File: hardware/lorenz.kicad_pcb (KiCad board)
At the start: 2 copper layers, 100 x 100 mm, 82 parts, among them J1 USB-C, J2 BNC, J3 BNC, J4 BNC, SW1 SW_DIP_x06, U1 LF412, U2 LF412, U3 MPY634, U4 MPY634, U5 A0515S-2WR2, U6 78L12, U7 79L12

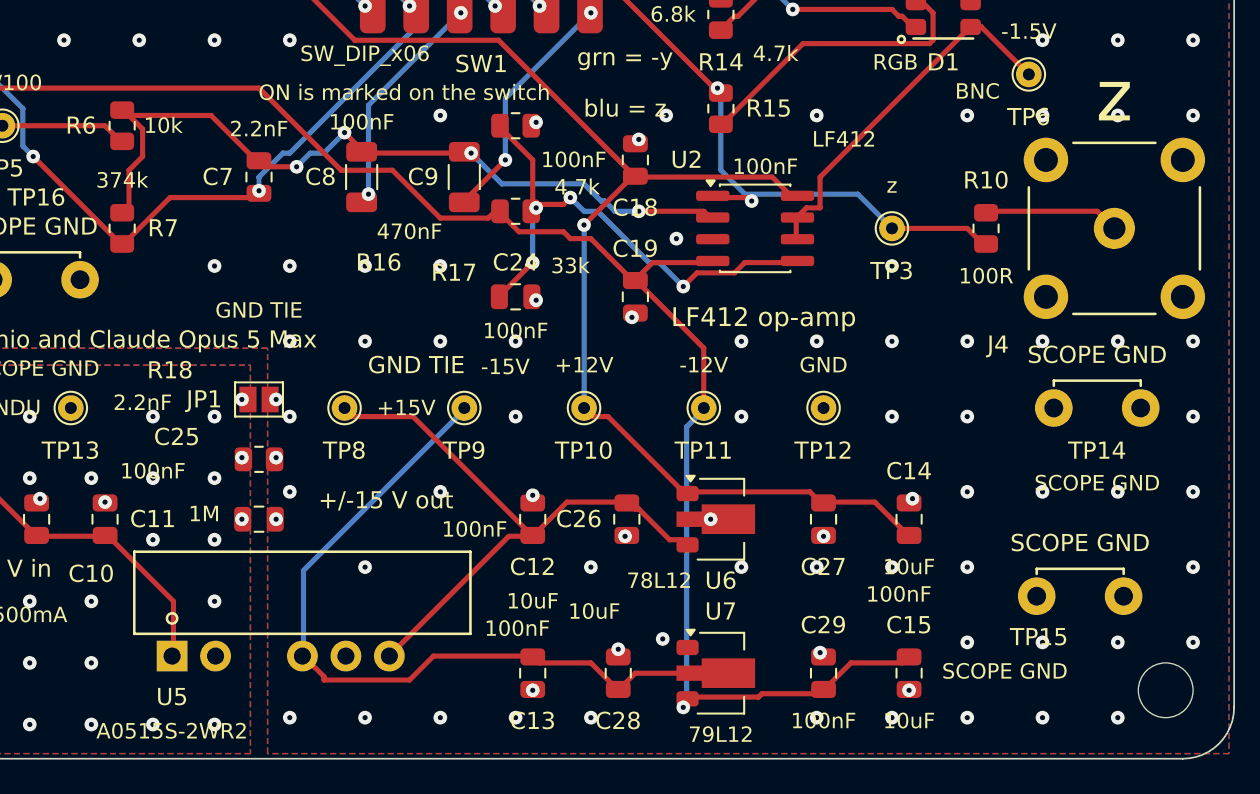
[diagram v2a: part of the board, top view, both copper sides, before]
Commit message: Give every probe pad its name directly above it
JP1's value already said GND TIE; the second label saying the same thing sat
on top of TP8's, which pushed +15V sideways and made the row ambiguous again.

Co-Authored-By: Claude Opus 5 <noreply@anthropic.com>
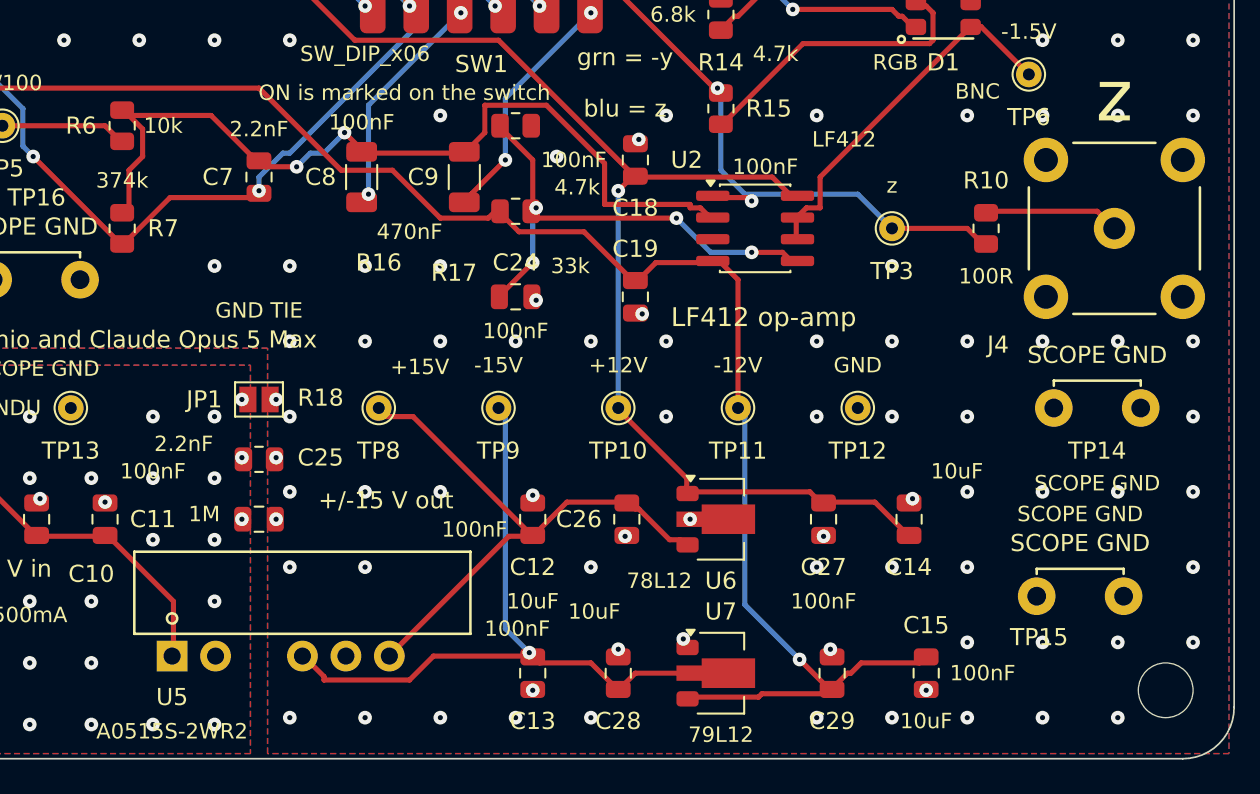
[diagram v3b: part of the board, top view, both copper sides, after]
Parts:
- moved TP10 2.00 mm to (64.0, 79.5)
- moved TP11 2.00 mm to (71.0, 79.5)
- moved TP12 2.00 mm to (78.0, 79.5)
- moved TP8 2.00 mm to (50.0, 79.5)
- moved TP9 2.00 mm to (57.0, 79.5)
- moved C15 1.00 mm to (82.0, 95.0)
- moved C29 0.50 mm to (76.5, 95.0)
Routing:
- net /SJ_Z: track 45.3 -> 50.0 mm, vias 4 -> 2
- net -15V: track 43.4 -> 40.3 mm, vias 0 -> 1
- net +12V: track 189.0 -> 186.7 mm
- net +15V: track 36.2 -> 34.2 mm
- net Net-(U2B-+): track 30.9 -> 29.0 mm
- net -12V: track 185.1 -> 186.6 mm
- net GND: vias 252 -> 253
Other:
- board text removed: "GND TIE"

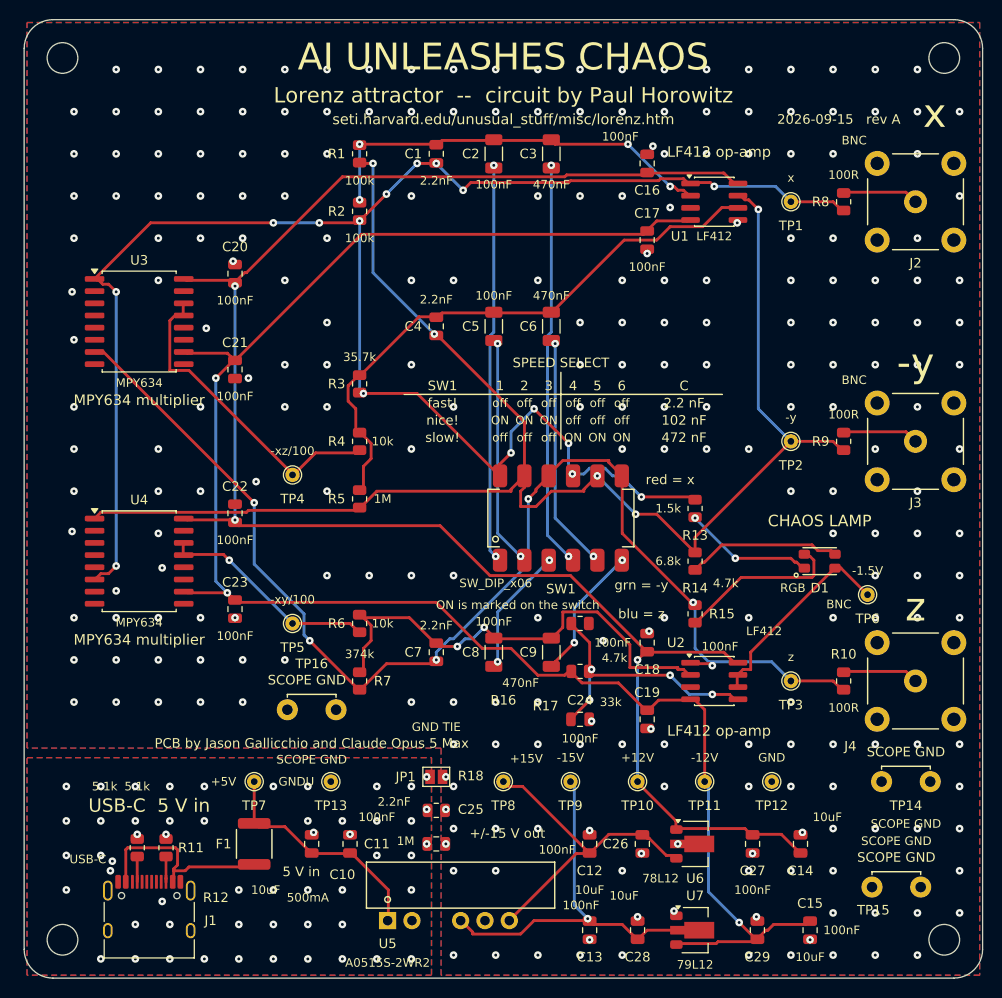
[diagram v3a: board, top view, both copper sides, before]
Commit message: Add an r knob and a sync input, and build the lamp as option 038
The lamp is now the common-anode MHPA3528CRGBCT held at +3.20 V by U2B,
with z -> red through 470R, x -> green through 3.9k and -y -> blue
through 1.5k: option 038 of the hundred renderings.  All three peaks land
within 8 % of each other, so the colour mixes instead of blinking.

R3 splits into 27k plus RV1, a Bourns 3386P 20k trimmer, sweeping
r = 21.3 to 37.0 across both bifurcations and Lorenz's 28.  Terminal 1 is
tied to the wiper, so grit under the wiper means maximum resistance and
the lowest r, never an open circuit.  check_circuit.py now solves the
whole board twice, once at each end of the knob, and checks r as a range.

A SYNC IN pad feeds the dy/dt summing junction through 100k, with 1M
holding it down when nothing is plugged in.  That junction is the only
one where an inverting input can still add to a term: drive it from
another board's x, turn the receiver's knob down by 10, and the two lock
in about five time units.  Pull the wire and they diverge again, which is
what the freeze switch was going to be for.

Also: a filled pin-1 triangle on every part that can be fitted turned,
drawn from the real pad and courtyard; every series resistor rotated
horizontal to match the schematic and every shunt vertical; the USB-C
moved 4 mm out so a cable with a moulded body can seat; a fourth speed
called "glacial!"; the x/y/z -> R/G/B mapping on the front silk beside
the lamp; URLs printed under both QR codes; and the back paragraph reset
one sentence per line across the foot of the board.

Co-Authored-By: Claude Opus 5 <noreply@anthropic.com>
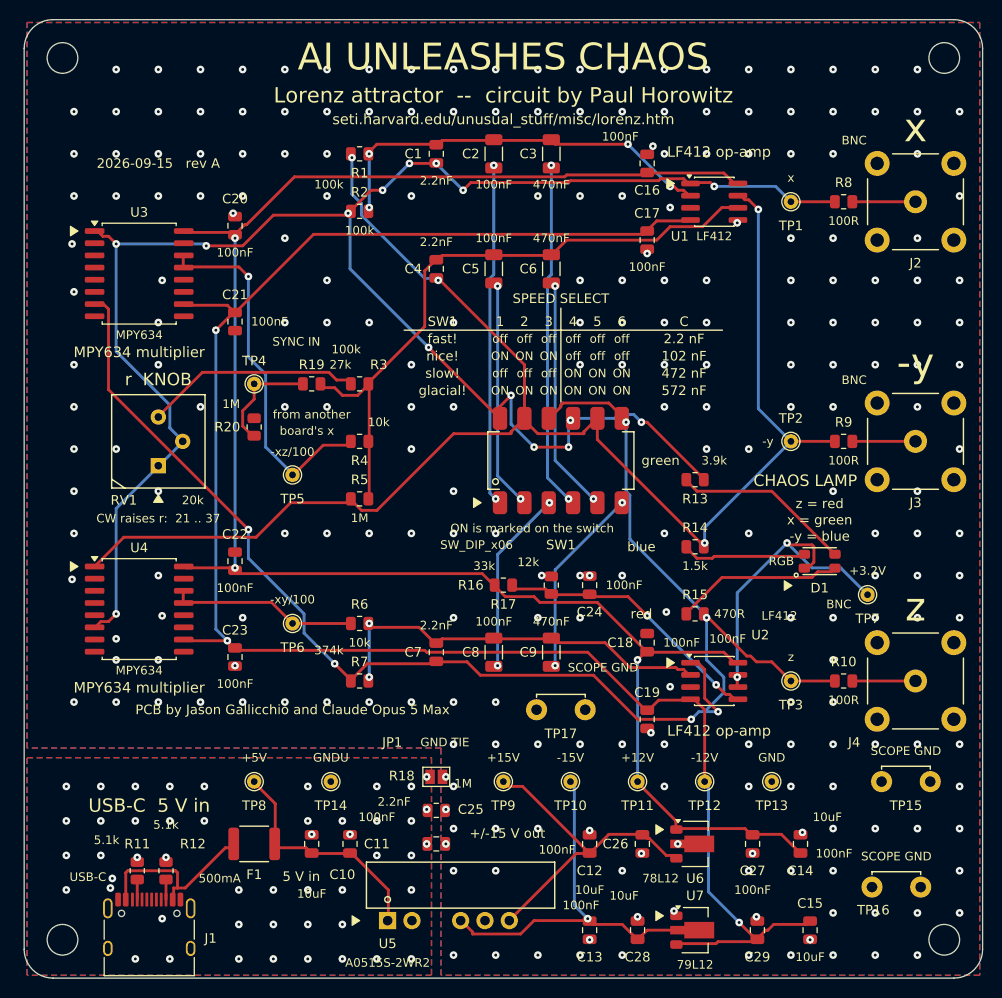
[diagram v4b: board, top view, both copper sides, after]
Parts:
- added R19: 100k, Resistor_SMD:R_0805_2012Metric, F.Cu at (30.0, 38.0)
- added R20: 1M, Resistor_SMD:R_0805_2012Metric, F.Cu at (24.0, 42.5)
- added RV1: 20k, lorenz:Potentiometer_Bourns_3386P_Vertical, F.Cu at (14.0, 46.5)
- added TP17: SCOPE GND, lorenz:TestPoint_ScopeGnd_Loop_2x1.1mm, F.Cu at (56.0, 72.0)
- R13: value 1.5k -> 3.9k
- R14: value 6.8k -> 1.5k
- R15: value 4.7k -> 470R
- R16: value 4.7k -> 12k
- R3: value 35.7k -> 27k
- TP10: value +12V -> -15V
- TP11: value -12V -> +12V
- TP12: value GND -> -12V
- TP13: value GNDU -> GND
- TP14: value SCOPE GND -> GNDU; footprint lorenz:TestPoint_ScopeGnd_Loop_2x1.1mm -> TestPoint:TestPoint_THTPad_D1.5mm_Drill0.7mm
- TP4: value -xz/100 -> SYNC IN
- TP5: value -xy/100 -> -xz/100
- TP6: value -1.5V -> -xy/100
- TP7: value +5V -> +3.2V
- TP8: value +15V -> +5V
- TP9: value -15V -> +15V
- moved TP7 66.9 mm to (88.0, 60.0)
- moved TP16 63.7 mm to (91.0, 90.5)
- moved TP6 60.1 mm to (28.0, 63.0)
- moved TP14 60.0 mm to (32.0, 79.5)
- moved TP13 46.0 mm to (78.0, 79.5)
- moved TP8 26.0 mm to (24.0, 79.5)
- moved TP5 15.5 mm to (28.0, 47.5)
- moved C24 14.0 mm to (59.0, 59.0), turned to 90 degrees
- moved R17 12.0 mm to (50.0, 59.0)
- moved TP15 11.0 mm to (92.0, 79.5)
- moved TP4 10.3 mm to (24.0, 38.0)
- moved TP10 7.00 mm to (57.0, 79.5)
- moved TP11 7.00 mm to (64.0, 79.5)
- moved TP12 7.00 mm to (71.0, 79.5)
- moved TP9 7.00 mm to (50.0, 79.5)
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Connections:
- D1 pad 1: Net-(D1-R) -> Net-(D1-A)
- D1 pad 4: Net-(D1-K) -> Net-(D1-R)
- R13 pad 1: Net-(D1-R) -> Net-(D1-G)
- R14 pad 1: Net-(D1-G) -> Net-(D1-B)
- R15 pad 1: Net-(D1-B) -> Net-(D1-R)
- R17 pad 1: -12V -> +12V
- R3 pad 1: /x -> Net-(R3-Pad1)
- TP10 pad 1: +12V -> -15V
- TP11 pad 1: -12V -> +12V
- TP12 pad 1: GND -> -12V
- TP13 pad 1: GNDU -> GND
- TP14 pad 1: GND -> GNDU
- TP4 pad 1: /xz -> Net-(R19-Pad1)
- TP5 pad 1: /xy -> /xz
- TP6 pad 1: Net-(D1-K) -> /xy
- TP7 pad 1: +5V -> Net-(D1-A)
- TP8 pad 1: +15V -> +5V
- TP9 pad 1: -15V -> +15V
- U2 pad 6: Net-(D1-K) -> Net-(D1-A)
- U2 pad 7: Net-(D1-K) -> Net-(D1-A)
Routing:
- net Net-(D1-A): track 0.00 -> 33.9 mm, vias 0 -> 2
- net /z: track 132.1 -> 161.7 mm
- net Net-(R3-Pad1): track 0.00 -> 22.6 mm
- net Net-(D1-K): track 21.7 -> 0.00 mm
- net Net-(R19-Pad1): track 0.00 -> 11.6 mm
- net /SJ_Z: track 50.0 -> 42.3 mm
- net /SJ_Y: track 60.8 -> 67.6 mm
- net Net-(C9-Pad1): track 14.2 -> 20.4 mm
- net Net-(C8-Pad1): track 13.5 -> 19.7 mm
- net Net-(C3-Pad1): track 42.8 -> 36.8 mm
- net Net-(C2-Pad1): track 42.1 -> 36.1 mm
- net +12V: track 186.7 -> 192.5 mm
- net -12V: track 186.6 -> 192.1 mm
- net /xz: track 33.6 -> 38.6 mm, vias 0 -> 1
- net /x: track 188.4 -> 192.8 mm, vias 16 -> 15
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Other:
- board text added: "-y = blue"
- board text added: "/ai_unleashes_chaos"
- board text added: "/misc/lorenz.htm"
- board text added: "572 nF"
- board text added: "CW raises r: 21 .. 37"
- board text added: "Every term weighs 1 MEG / R."
- board text added: "Signals are 0.1 V per unit, and the time scale is tau = 1 MEG x C."
- board text added: "The MPY634s form A*B/10, and both minus signs come from swapped inputs."
- board text added: "blue"
- board text added: "board's x"
- board text added: "from another"
- board text added: "github.com/gallicchio"
- board text added: "glacial!"
- board text added: "green"
- board text added: "put x and z on X-Y to see this"
- board text added: "r KNOB"
- board text added: "r is R3 = 27k plus the knob RV1, which sweeps r from 21 to 37."
- board text added: "red"
- board text added: "s = 10 r = 21 to 37 b = 8/3"
- board text added: "s is R1 = R2 = 100k, and b is R7 = 374k."
- board text added: "seti.harvard.edu/unusual_stuff"
- board text added: "x = green"
- board text added: "z = red"
- board text removed: "100k is s, R3 = 35.7k is r, R7 = 374k is b."
- board text removed: "Every term weighs 1 MEG / R: R1 = R2 ="
- board text removed: "SCOPE GND"
- board text removed: "The MPY634s form A*B/10 and take their"
- board text removed: "blu = z"
- board text removed: "grn = -y"
- board text removed: "minus signs from swapped inputs. 0.1 V"
- board text removed: "per unit; time scale tau = 1 MEG x C."
- board text removed: "red = x"
- board text removed: "s = 10 r = 28 b = 8/3"
- board text removed: "seti.harvard.edu"
- board text removed: "x and z on a scope in X-Y draw this"
